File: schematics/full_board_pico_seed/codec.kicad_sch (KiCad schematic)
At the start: 18 parts, among them U2 PCM3060PWR, X1 SG-5032CAN 12.288MHz

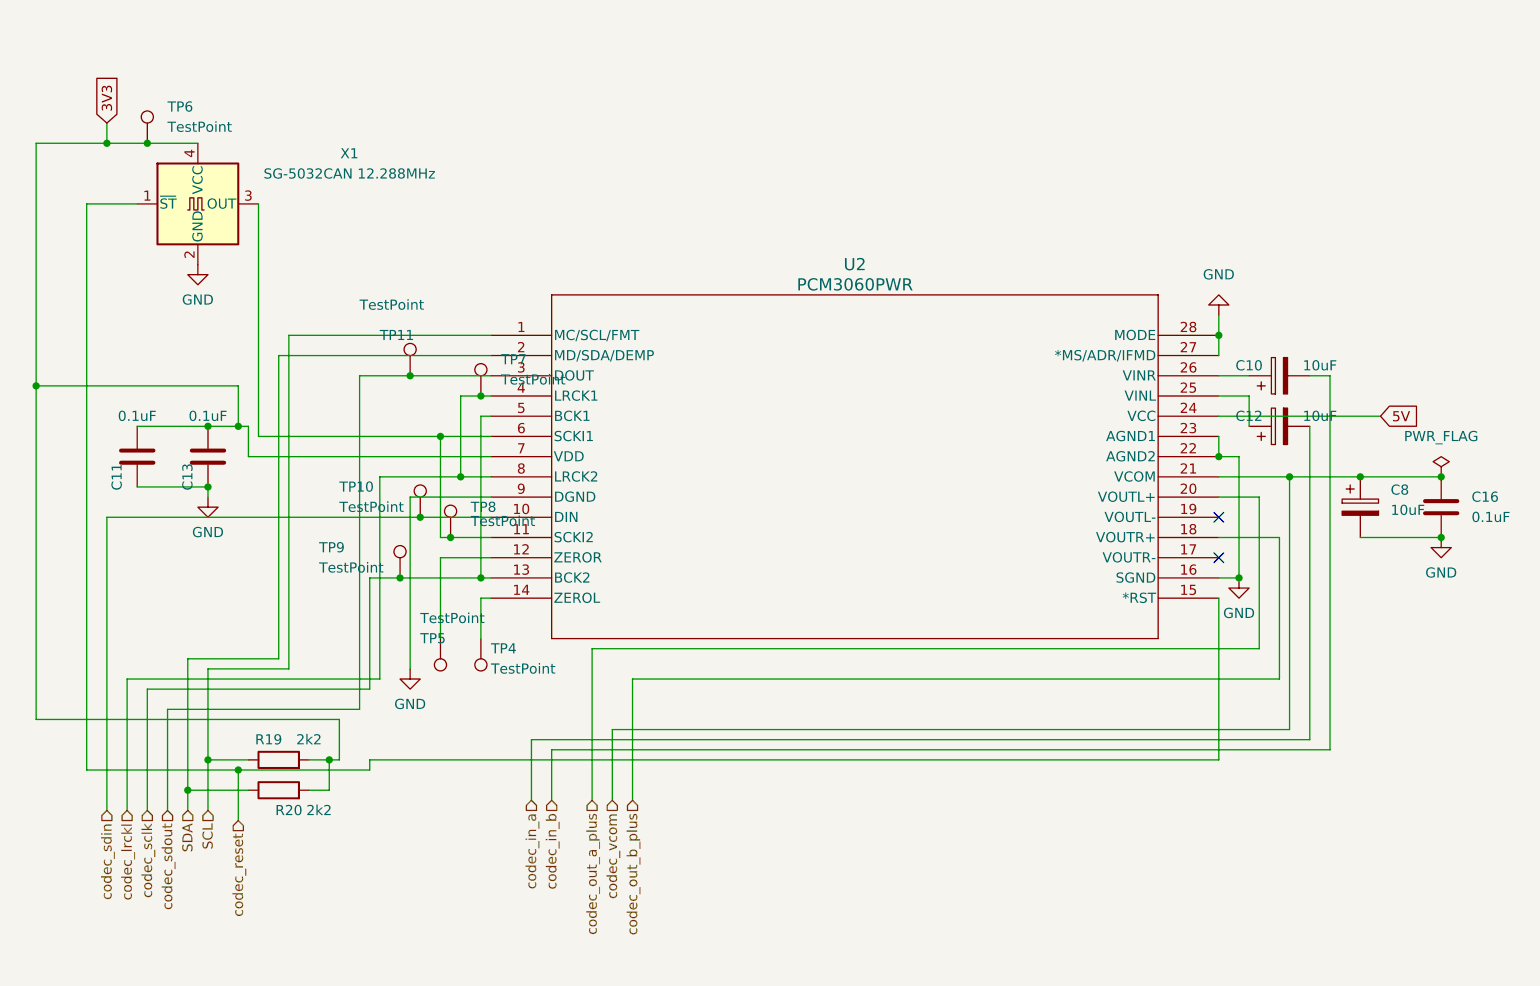
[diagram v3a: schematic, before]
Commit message: exchanged incorrect pcm3060 symbol, cleaned symbol table
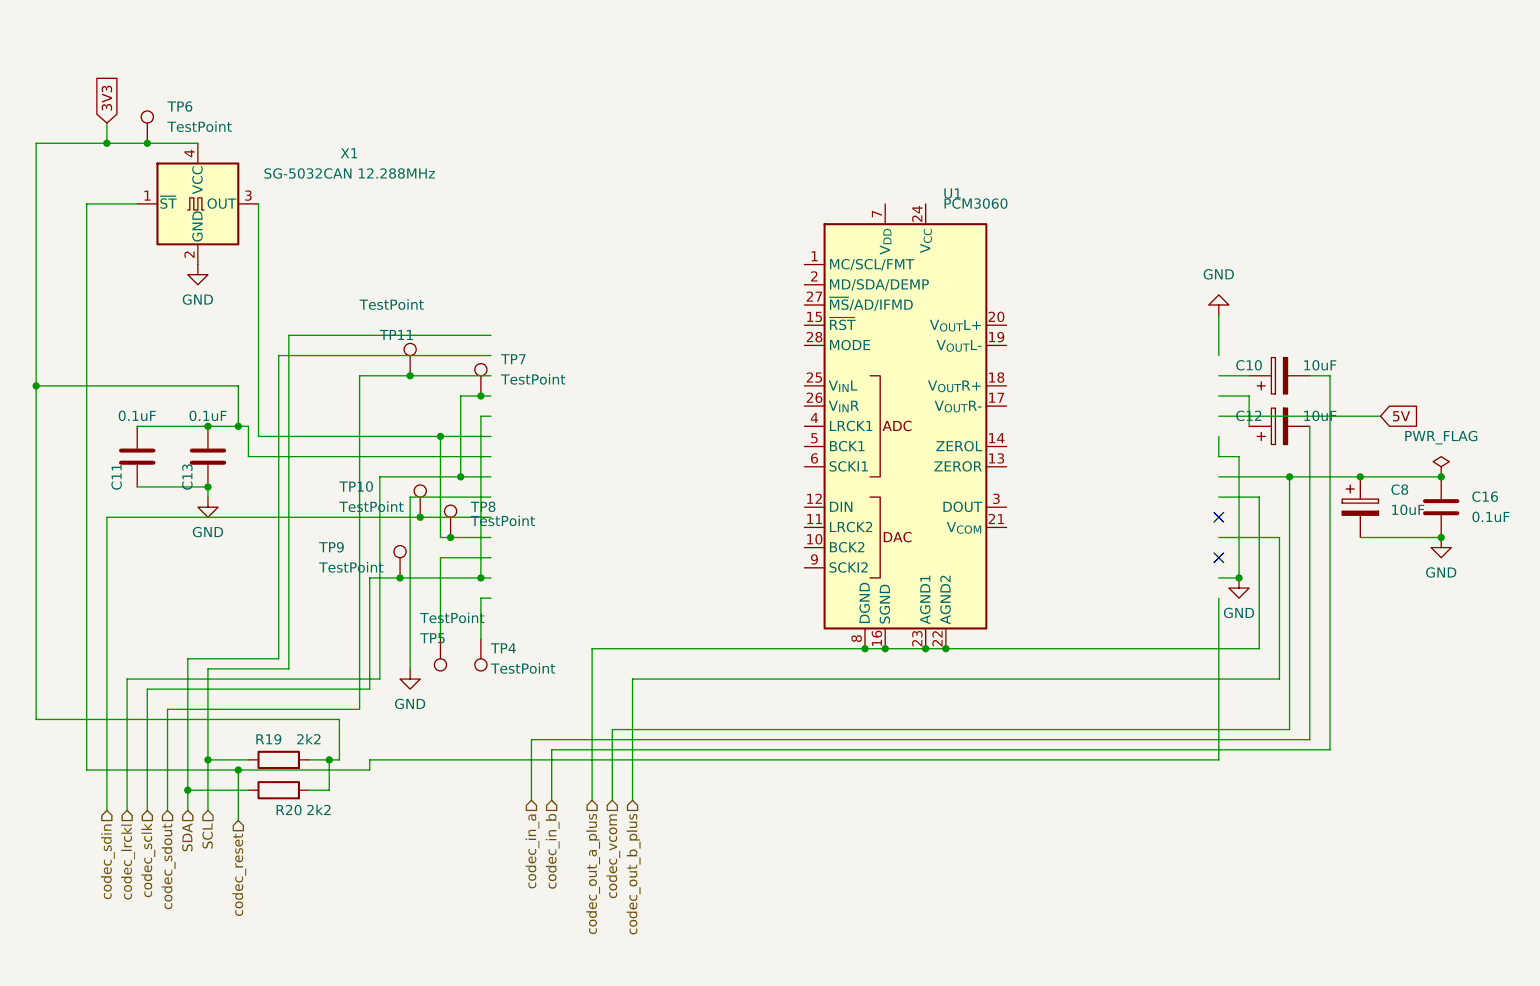
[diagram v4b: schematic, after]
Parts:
- removed U2: PCM3060PWR, Package_SO:TSSOP-28_4.4x9.7mm_P0.65mm, symbol pcm3060:PCM3060PWR
- added U1: PCM3060, Package_SO:TSSOP-28_4.4x9.7mm_P0.65mm, symbol Audio:PCM3060
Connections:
- net codec_out_a_plus: now also U1.16 (SGND), U1.22 (AGND2), U1.23 (AGND1), U1.8 (DGND)
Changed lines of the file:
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@@
+	)
+	(junction
+		(at 184.15 102.87)
+		(diameter 0)
+		(color 0 0 0 0)
 	)
 	(junction
@@
 	)
 	(junction
+		(at 189.23 102.87)
+		(diameter 0)
+		(color 0 0 0 0)
+	)
+	(junction
+		(at 191.77 102.87)
+		(diameter 0)
+		(color 0 0 0 0)
+	)
+	(junction
 		(at 96.52 120.65)
 		(diameter 0)
@@
 	)
 	(junction
-		(at 226.06 78.74)
-		(diameter 0)
-		(color 0 0 0 0)
-	)
-	(junction
 		(at 114.3 116.84)
 		(diameter 0)
@@
 	)
 	(junction
-		(at 226.06 63.5)
-		(diameter 0)
-		(color 0 0 0 0)
-	)
-	(junction
 		(at 77.47 69.85)
 		(diameter 0)
@@
 	(junction
 		(at 243.84 81.28)
+		(diameter 0)
+		(color 0 0 0 0)
+	)
+	(junction
+		(at 181.61 102.87)
 		(diameter 0)
 		(color 0 0 0 0)
@@
 	(wire
 		(pts
-			(xy 226.06 63.5) (xy 226.06 66.04)
+			(xy 226.06 60.96) (xy 226.06 66.04)
 		)
 		(stroke
@@
 	(wire
 		(pts
+			(xy 184.15 102.87) (xy 189.23 102.87)
+		)
+		(stroke
+			(width 0)
+			(type default)
+		)
+	)
+	(wire
+		(pts
 			(xy 134.62 91.44) (xy 128.27 91.44)
 		)
@@
 	(wire
 		(pts
+			(xy 181.61 102.87) (xy 184.15 102.87)
+		)
+		(stroke
+			(width 0)
+			(type default)
+		)
+	)
+	(wire
+		(pts
 			(xy 119.38 118.11) (xy 102.87 118.11)
 		)
@@
 	(wire
 		(pts
-			(xy 226.06 60.96) (xy 226.06 63.5)
-		)
-		(stroke
-			(width 0)
-			(type default)
-		)
-	)
-	(wire
-		(pts
 			(xy 96.52 120.65) (xy 104.14 120.65)
 		)
@@
 	(wire
 		(pts
+			(xy 191.77 102.87) (xy 231.14 102.87)
+		)
+		(stroke
+			(width 0)
+			(type default)
+		)
+	)
+	(wire
+		(pts
 			(xy 97.79 39.37) (xy 91.44 39.37)
 		)
@@
 	(wire
 		(pts
+			(xy 189.23 102.87) (xy 191.77 102.87)
+		)
+		(stroke
+			(width 0)
+			(type default)
+		)
+	)
+	(wire
+		(pts
 			(xy 128.27 76.2) (xy 134.62 76.2)
 		)
@@
 	(wire
 		(pts
-			(xy 147.32 102.87) (xy 231.14 102.87)
+			(xy 147.32 102.87) (xy 181.61 102.87)
 		)
 		(stroke
@@
 	)
 	(symbol
+		(lib_id "Audio:PCM3060")
+		(at 186.69 74.93 0)
+		(unit 1)
+		(exclude_from_sim no)
+		(in_bom yes)
+		(on_board yes)
+		(dnp no)
+		(fields_autoplaced yes)
+		(property "Reference" "U1"
+			(at 191.4241 45.72 0)
+			(effects
+				(font
+					(size 1.27 1.27)
+				)
+				(justify left)
+			)
+		)
+		(property "Value" "PCM3060"
+			(at 191.4241 46.99 0)
+			(effects
+				(font
+					(size 1.27 1.27)
+				)
+				(justify left)
+			)
+		)
+		(property "Footprint" "Package_SO:TSSOP-28_4.4x9.7mm_P0.65mm"
+			(at 186.69 117.348 0)
+			(effects
+				(font
+					(size 1.27 1.27)
+				)
+				(hide yes)
+			)
+		)
+		(property "Datasheet" "https://www.ti.com/lit/gpn/pcm3060"
+			(at 186.69 114.554 0)
+			(effects
+				(font
+					(size 1.27 1.27)
+				)
+				(hide yes)
+			)
+		)
+		(property "Description" "24-bit Asynchronous Stereo Audio Codec with 96/192kHz sampling rate, TSSOP-28"
+			(at 185.674 119.888 0)
+			(effects
+				(font
+					(size 1.27 1.27)
+				)
+				(hide yes)
+			)
+		)
+		(pin "22"
+		)
+		(pin "5"
+		)
+		(pin "1"
+		)
+		(pin "12"
+		)
+		(pin "10"
+		)
+		(pin "21"
+		)
+		(pin "15"
+		)
+		(pin "13"
+		)
+		(pin "14"
+		)
+		(pin "26"
+		)
+		(pin "23"
+		)
+		(pin "27"
+		)
+		(pin "28"
+		)
+		(pin "11"
+		)
+		(pin "4"
+		)
+		(pin "16"
+		)
+		(pin "19"
+		)
+		(pin "7"
+		)
+		(pin "8"
+		)
+		(pin "6"
+		)
+		(pin "24"
+		)
+		(pin "17"
+		)
+		(pin "3"
+		)
+		(pin "20"
+		)
+		(pin "9"
+		)
+		(pin "2"
+		)
+		(pin "25"
+		)
+		(pin "18"
+		)
+		(instances
+			(project ""
+				(path "/e63e39d7-6ac0-4ffd-8aa3-1841a4541b55/6ec17984-49ce-45c2-b1f4-ed6e904b8c80"
+					(reference "U1")
+					(unit 1)
+				)
+			)
+		)
+	)
+	(symbol
 		(lib_id "power:GND")
 		(at 97.79 54.61 0)
@@
 					(unit 1)
 				)
-			)
-		)
-	)
-	(symbol
-		(lib_id "pcm3060:PCM3060PWR")
-		(at 134.62 63.5 0)
-		(unit 1)
-		(exclude_from_sim no)
-		(in_bom yes)
-		(on_board yes)
-		(dnp no)
-		(fields_autoplaced yes)
-		(property "Reference" "U2"
-			(at 180.34 54.61 0)
-			(effects
-				(font
-					(size 1.524 1.524)
-				)
-			)
-		)
-		(property "Value" "PCM3060PWR"
-			(at 180.34 57.15 0)
-			(effects
-				(font
-					(size 1.524 1.524)
-				)
-			)
-		)
-		(property "Footprint" "Package_SO:TSSOP-28_4.4x9.7mm_P0.65mm"
-			(at 134.62 63.5 0)
-			(effects
-				(font
-					(size 1.27 1.27)
-					(italic yes)
-				)
-				(hide yes)
-			)
-		)
-		(property "Datasheet" "PCM3060PWR"
-			(at 134.62 63.5 0)
-			(effects
-				(font
-					(size 1.27 1.27)
-					(italic yes)
-				)
-				(hide yes)
-			)
-		)
-		(property "Description" ""
-			(at 134.62 63.5 0)
-			(effects
-				(font
-					(size 1.27 1.27)
-				)
-				(hide yes)
-			)
-		)
-		(pin "19"
-		)
-		(pin "27"
-		)
-		(pin "3"
-		)
-		(pin "4"
-		)
-		(pin "10"
-		)
-		(pin "1"
-		)
-		(pin "6"
-		)
-		(pin "8"
-		)
-		(pin "25"
-		)
-		(pin "18"
-		)
-		(pin "5"
-		)
-		(pin "11"
-		)
-		(pin "9"
-		)
-		(pin "21"
-		)
-		(pin "23"
-		)
-		(pin "20"
-		)
-		(pin "14"
-		)
-		(pin "15"
-		)
-		(pin "22"
-		)
-		(pin "26"
-		)
-		(pin "2"
-		)
-		(pin "28"
-		)
-		(pin "13"
-		)
-		(pin "24"
-		)
-		(pin "17"
-		)
-		(pin "7"
-		)
-		(pin "16"
-		)
-		(pin "12"
-		)
-		(instances
-			(project "full_board_pico_seed"
-				(path "/e63e39d7-6ac0-4ffd-8aa3-1841a4541b55/6ec17984-49ce-45c2-b1f4-ed6e904b8c80"
-					(reference "U2")
-					(unit 1)
-				)

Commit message: corrected schematic regarding pcm3060
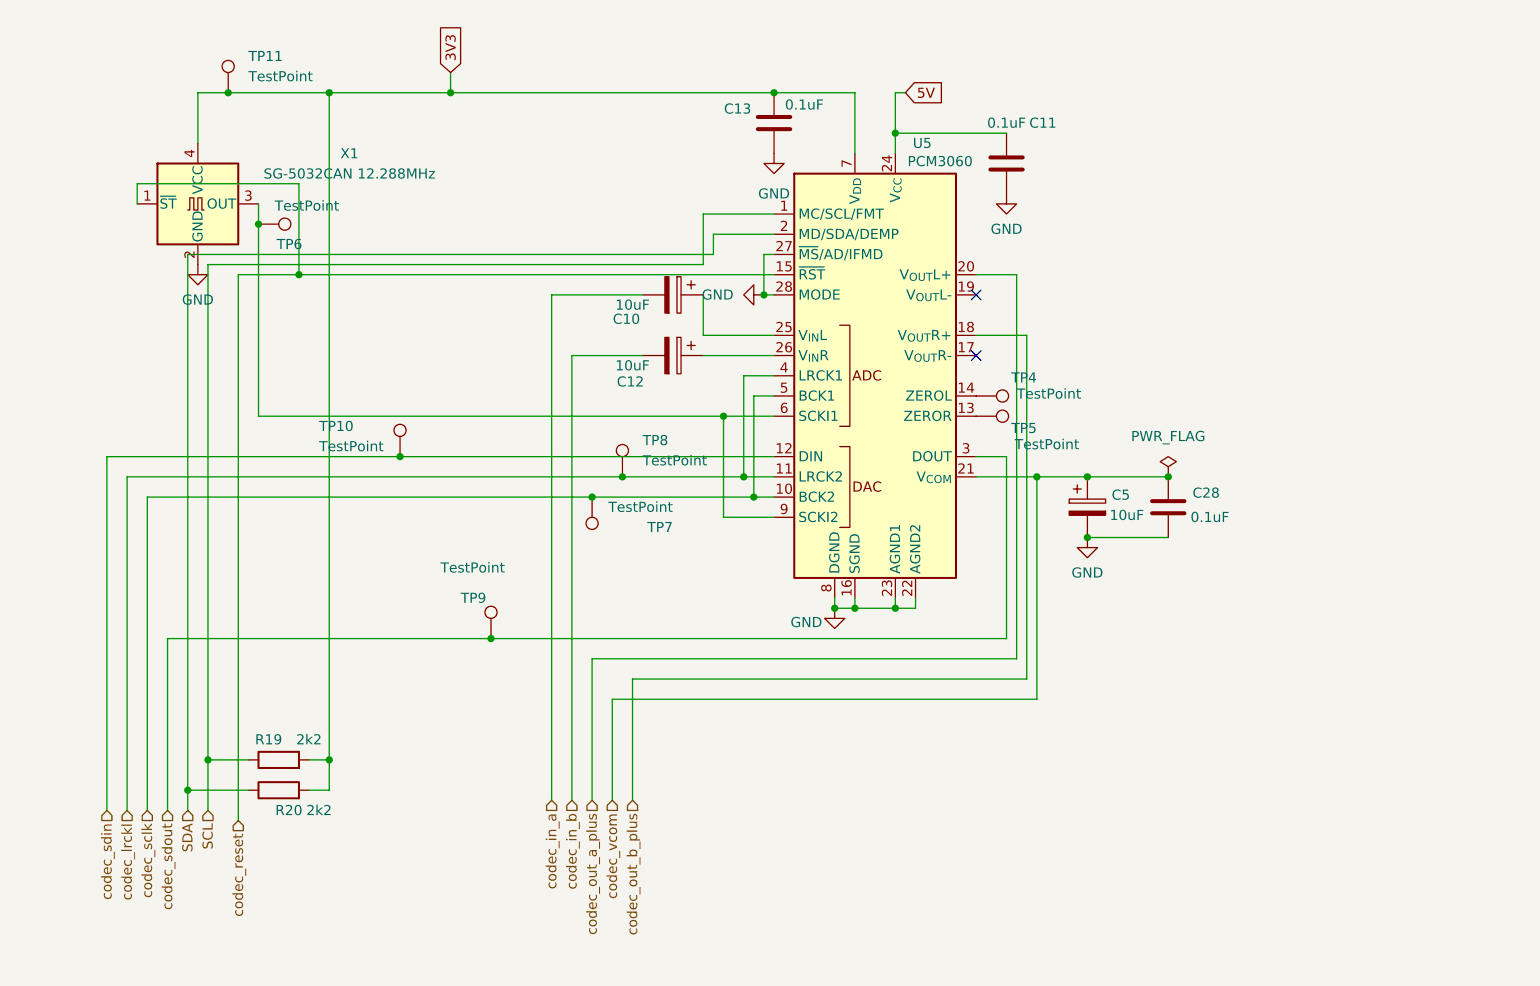
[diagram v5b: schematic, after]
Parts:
- renumbered C16 to C28, C8 to C5, TP6 to TP11, TP8 to TP6, TP9 to TP7, TP7 to TP8, TP11 to TP9, U1 to U5
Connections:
- net 3V3: now also U5.7 (V_{DD}); no longer C11.1
- net 5V: now also C11.1, U5.24 (V_{CC})
- net GND: now also U5.16 (SGND), U5.22 (AGND2), U5.23 (AGND1), U5.27 (~{MS}/AD/IFMD), U5.28 (MODE), U5.8 (DGND)
- net SCL: now also U5.1 (MC/SCL/FMT)
- net SDA: now also U5.2 (MD/SDA/DEMP)
- net codec_in_a: now also C10.2; no longer C12.2
- net codec_in_b: now also C12.2; no longer C10.2
- net codec_lrckl: now also U5.11 (LRCK2), U5.4 (LRCK1)
- net codec_out_a_plus: now also U5.20 (V_{OUT}L+); no longer U5.16 (SGND), U5.22 (AGND2), U5.23 (AGND1), U5.8 (DGND)
- net codec_out_b_plus: now also U5.18 (V_{OUT}R+)
- net codec_reset: now also U5.15 (~{RST})
- net codec_sclk: now also U5.10 (BCK2), U5.5 (BCK1)
- net codec_sdin: now also U5.12 (DIN)
- net codec_sdout: now also U5.3 (DOUT)
- net codec_vcom: now also U5.21 (V_{COM})
- net at U5.13 (ZEROR): now also TP5.1
- net at U5.14 (ZEROL): now also TP4.1
- net at U5.25 (V_{IN}L): now also C10.1
- net at U5.26 (V_{IN}R): now also C12.1
- net at U5.6 (SCKI1): now also TP6.1, U5.9 (SCKI2), X1.3 (OUT)
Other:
- moved on the sheet: C10, C11, C12, C13, C28, C5, TP10, TP11, TP4, TP5, TP6, TP7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
